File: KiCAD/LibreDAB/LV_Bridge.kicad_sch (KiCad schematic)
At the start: 68 parts, among them J1 HX PM2.54-1X4P TP H8.5-ZQ, J2 TS30050050-040, J3 TS30050050-040, J4 HX PM2.54-1X4P TP H8.5-ZQ, J5 HX PM2.54-1X4P TP H8.5-ZQ, J6 HX PM2.54-1X4P TP H8.5-ZQ, J7 TS30050050-040, J8 TS30050050-040, Q1 SP010N01BGHTO, Q2 SP010N01BGHTO, Q3 SP010N01BGHTO, Q4 SP010N01BGHTO, U2 10 MHz Opamp, U3 10 MHz Opamp, U4 10 MHz Opamp

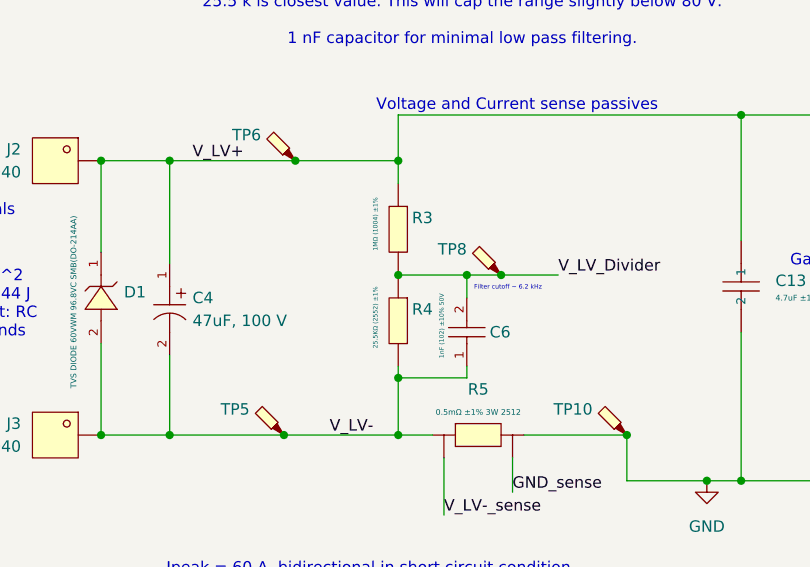
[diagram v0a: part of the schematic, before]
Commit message: Updated Voltage divider to 1206 for top half and 0.1%
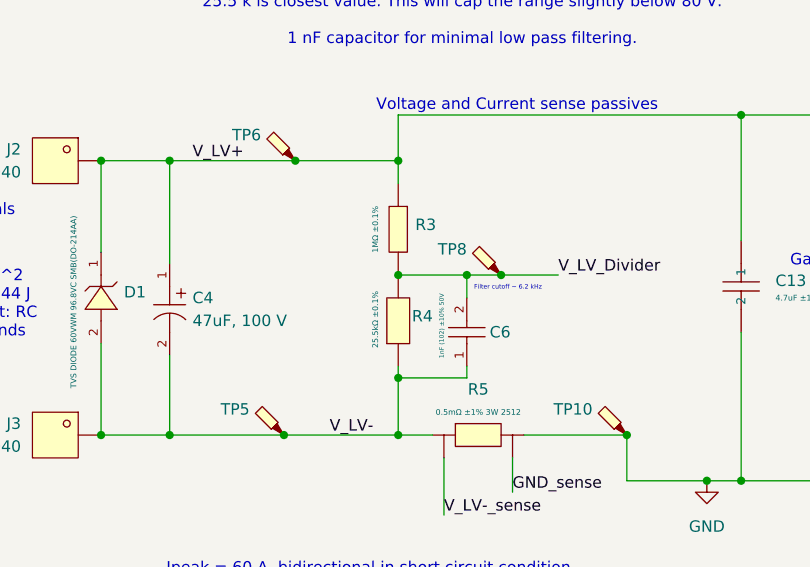
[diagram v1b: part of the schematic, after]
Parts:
- removed R3: 1MΩ (1004) ±1%, lcsc_footprints:C17514_R0805, symbol lcsc_imported:1MΩ_(1004)_±1%
- removed R4: 25.5KΩ (2552) ±1%, lcsc_footprints:C46670_R0805, symbol lcsc_imported:25_5KΩ_(2552)_±1%
- added R3: 1MΩ ±0.1%, lcsc_footprints:C309662_R1206, symbol lcsc_imported:RES 1MΩ ±0.1% 250mW 1206
- added R4: 25.5kΩ ±0.1%, lcsc_footprints:C865332_R0805, symbol lcsc_imported:RES 25.5kΩ ±0.1% 125mW 0805
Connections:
- net V_LV+: now also R3.1
- net V_LV-: now also R4.1
- net V_LV_Divider: now also R3.2, R4.2
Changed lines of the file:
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@@
 	)
 	(symbol
-		(lib_id "lcsc_imported:25_5KΩ_(2552)_±1%")
-		(at 82.55 81.28 270)
-		(unit 1)
-		(exclude_from_sim no)
-		(in_bom yes)
-		(on_board yes)
-		(dnp no)
-		(property "Reference" "R4"
-			(at 84.074 80.01 90)
-			(effects
-				(font
-					(size 1.27 1.27)
-				)
-				(justify left)
-			)
-		)
-		(property "Value" "25.5KΩ (2552) ±1%"
-			(at 80.01 77.47 0)
-			(effects
-				(font
-					(size 0.5 0.5)
-				)
-				(justify left)
-			)
-		)
-		(property "Footprint" "lcsc_footprints:C46670_R0805"
-			(at 72.39 81.28 0)
-			(effects
-				(font
-					(size 1.27 1.27)
-				)
-				(hide yes)
-			)
-		)
-		(property "Datasheet" "https://www.lcsc.com/datasheet/lcsc_datasheet_2206010000_UNI-ROYAL-Uniroyal-Elec-0805W8F2552T5E_C46670.pdf"
-			(at 82.677 78.994 0)
-			(effects
-				(font
-					(size 1.27 1.27)
-				)
-				(hide yes)
-			)
-		)
-		(property "Description" "25.5KΩ (2552) ±1%"
-			(at 82.55 81.28 0)
-			(effects
-				(font
-					(size 1.27 1.27)
-				)
-				(hide yes)
-			)
-		)
-		(property "LCSC" "C46670"
-			(at 82.55 81.28 0)
-			(effects
-				(font
-					(size 1.27 1.27)
-				)
-				(hide yes)
-			)
-		)
-		(property "Manufacturer" "UNI-ROYAL(厚声)"
-			(at 82.55 81.28 0)
-			(effects
-				(font
-					(size 1.27 1.27)
-				)
-				(hide yes)
-			)
-		)
-		(pin "1"
-		)
-		(pin "2"
-		)
-		(instances
-			(project "LibreDAB"
-				(path "/daf77073-b189-4351-8636-4e7a5198e1b7/f3c2518b-d41d-4c2c-ab2c-6739c5137e70"
-					(reference "R4")
-					(unit 1)
-				)
-			)
-		)
-	)
-	(symbol
 		(lib_id "lcsc_imported:HX_PM2_54-1X4P_TP_H8_5-ZQ")
 		(at 71.12 21.59 0)
@@
 	)
 	(symbol
+		(lib_id "lcsc_imported:RES 1MΩ ±0.1% 250mW 1206")
+		(at 82.55 71.12 270)
+		(unit 1)
+		(exclude_from_sim no)
+		(in_bom yes)
+		(on_board yes)
+		(dnp no)
+		(property "Reference" "R3"
+			(at 85.598 70.612 90)
+			(effects
+				(font
+					(size 1.27 1.27)
+				)
+			)
+		)
+		(property "Value" "1MΩ ±0.1%"
+			(at 80.01 71.12 0)
+			(effects
+				(font
+					(size 0.635 0.635)
+				)
+			)
+		)
+		(property "Footprint" "lcsc_footprints:C309662_R1206"
+			(at 72.39 71.12 0)
+			(effects
+				(font
+					(size 1.27 1.27)
+				)
+				(hide yes)
+			)
+		)
+		(property "Datasheet" "https://wmsc.lcsc.com/wmsc/upload/file/pdf/v2/lcsc/2304140030_YAGEO-RT1206BRD071ML_C309662.pdf"
+			(at 82.677 68.834 0)
+			(effects
+				(font
+					(size 1.27 1.27)
+				)
+				(hide yes)
+			)
+		)
+		(property "Description" "RT1206BRD071ML"
+			(at 82.55 71.12 0)
+			(effects
+				(font
+					(size 1.27 1.27)
+				)
+				(hide yes)
+			)
+		)
+		(property "LCSC" "C309662"
+			(at 82.55 71.12 0)
+			(effects
+				(font
+					(size 1.27 1.27)
+				)
+				(hide yes)
+			)
+		)
+		(property "Manufacturer" "YAGEO(国巨)"
+			(at 82.55 71.12 0)
+			(effects
+				(font
+					(size 1.27 1.27)
+				)
+				(hide yes)
+			)
+		)
+		(pin "2"
+		)
+		(pin "1"
+		)
+		(instances
+			(project ""
+				(path "/daf77073-b189-4351-8636-4e7a5198e1b7/f3c2518b-d41d-4c2c-ab2c-6739c5137e70"
+					(reference "R3")
+					(unit 1)
+				)
+			)
+		)
+	)
+	(symbol
 		(lib_id "power:GND")
 		(at 128.27 22.86 0)
@@
 	)
 	(symbol
-		(lib_id "lcsc_imported:1MΩ_(1004)_±1%")
-		(at 82.55 71.12 270)
-		(unit 1)
-		(exclude_from_sim no)
-		(in_bom yes)
-		(on_board yes)
-		(dnp no)
-		(property "Reference" "R3"
-			(at 84.074 69.85 90)
-			(effects
-				(font
-					(size 1.27 1.27)
-				)
-				(justify left)
-			)
-		)
-		(property "Value" "1MΩ (1004) ±1%"
-			(at 80.01 67.564 0)
-			(effects
-				(font
-					(size 0.5 0.5)
-				)
-				(justify left)
-			)
-		)
-		(property "Footprint" "lcsc_footprints:C17514_R0805"
-			(at 72.39 71.12 0)
-			(effects
-				(font
-					(size 1.27 1.27)
-				)
-				(hide yes)
-			)
-		)
-		(property "Datasheet" "https://www.lcsc.com/datasheet/lcsc_datasheet_2206010200_UNI-ROYAL-Uniroyal-Elec-0805W8F1004T5E_C17514.pdf"
-			(at 82.677 68.834 0)
-			(effects
-				(font
-					(size 1.27 1.27)
-				)
-				(hide yes)
-			)
-		)
-		(property "Description" "1MΩ (1004) ±1%"
-			(at 82.55 71.12 0)
-			(effects
-				(font
-					(size 1.27 1.27)
-				)
-				(hide yes)
-			)
-		)
-		(property "LCSC" "C17514"
-			(at 82.55 71.12 0)
-			(effects
-				(font
-					(size 1.27 1.27)
-				)
-				(hide yes)
-			)
-		)
-		(property "Manufacturer" "UNI-ROYAL(厚声)"
-			(at 82.55 71.12 0)
-			(effects
-				(font
-					(size 1.27 1.27)
-				)
-				(hide yes)
-			)
-		)
-		(pin "1"
-		)
-		(pin "2"
-		)
-		(instances
-			(project "LibreDAB"
-				(path "/daf77073-b189-4351-8636-4e7a5198e1b7/f3c2518b-d41d-4c2c-ab2c-6739c5137e70"
-					(reference "R3")
-					(unit 1)
-				)
-			)
-		)
-	)
-	(symbol
 		(lib_id "Connector:TestPoint_Probe")
 		(at 137.16 88.9 0)
@@
 					(unit 1)
 				)
+			)
+		)
+	)
+	(symbol
+		(lib_id "lcsc_imported:RES 25.5kΩ ±0.1% 125mW 0805")
+		(at 82.55 81.28 90)
+		(unit 1)
+		(exclude_from_sim no)
+		(in_bom yes)
+		(on_board yes)
+		(dnp no)
+		(property "Reference" "R4"
+			(at 84.074 80.772 90)
+			(effects
+				(font
+					(size 1.27 1.27)
+				)
+				(justify right)
+			)
+		)
+		(property "Value" "25.5kΩ ±0.1%"
+			(at 80.01 77.978 0)
+			(effects
+				(font
+					(size 0.635 0.635)
+				)
+				(justify right)
+			)
+		)
+		(property "Footprint" "lcsc_footprints:C865332_R0805"
+			(at 92.71 81.28 0)
+			(effects
+				(font
+					(size 1.27 1.27)
+				)
+				(hide yes)
+			)
+		)
+		(property "Datasheet" "https://wmsc.lcsc.com/wmsc/upload/file/pdf/v2/lcsc/2210081801_YAGEO-RT0805BRD0725K5L_C865332.pdf"
+			(at 82.423 83.566 0)
+			(effects
+				(font
+					(size 1.27 1.27)
+				)
+				(hide yes)
+			)
+		)
+		(property "Description" "RT0805BRD0725K5L"
+			(at 82.55 81.28 0)
+			(effects
+				(font
+					(size 1.27 1.27)
+				)
+				(hide yes)
+			)
+		)
+		(property "LCSC" "C865332"
+			(at 82.55 81.28 0)
+			(effects
+				(font
+					(size 1.27 1.27)
+				)
+				(hide yes)
+			)
+		)
+		(property "Manufacturer" "YAGEO(国巨)"
+			(at 82.55 81.28 0)
+			(effects
+				(font
+					(size 1.27 1.27)
+				)
+				(hide yes)
+			)
+		)
+		(pin "1"
+		)
+		(pin "2"
+		)
+		(instances
+			(project ""
+				(path "/daf77073-b189-4351-8636-4e7a5198e1b7/f3c2518b-d41d-4c2c-ab2c-6739c5137e70"
+					(reference "R4")
+					(unit 1)
+				)

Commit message: Review comments addressed or parked
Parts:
- H1, H2, H3, H4: footprint 1Footprints:MountingHole_Pad_SMD_BD5.6-D4.1 -> MountingHole:MountingHole_4.3mm_M4_DIN965_Pad
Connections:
- net V_LV-: now also R4.2; no longer R4.1
- net V_LV_Divider: now also R4.1; no longer R4.2
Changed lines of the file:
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@@
 	)
 	(junction
-		(at 82.55 76.2)
-		(diameter 0)
-		(color 0 0 0 0)
-	)
-	(junction
 		(at 26.6567 20.32)
 		(diameter 0)
@@
 	)
 	(junction
-		(at 82.55 87.63)
-		(diameter 0)
-		(color 0 0 0 0)
-	)
-	(junction
 		(at 177.8 153.67)
 		(diameter 0)
@@
 	)
 	(junction
+		(at 82.55 87.63)
+		(diameter 0)
+		(color 0 0 0 0)
+	)
+	(junction
 		(at 212.09 88.9)
 		(diameter 0)
@@
 	)
 	(junction
+		(at 82.55 76.2)
+		(diameter 0)
+		(color 0 0 0 0)
+	)
+	(junction
 		(at 57.15 63.5)
 		(diameter 0)
@@
 	(wire
 		(pts
+			(xy 82.55 86.36) (xy 82.55 87.63)
+		)
+		(stroke
+			(width 0)
+			(type default)
+		)
+	)
+	(wire
+		(pts
 			(xy 128.27 153.67) (xy 138.43 153.67)
 		)
@@
 	(wire
 		(pts
-			(xy 82.55 86.36) (xy 82.55 87.63)
-		)
-		(stroke
-			(width 0)
-			(type default)
-		)
-	)
-	(wire
-		(pts
 			(xy 196.85 24.13) (xy 199.39 24.13)
 		)
@@
 			)
 		)
-		(property "Footprint" "1Footprints:MountingHole_Pad_SMD_BD5.6-D4.1"
+		(property "Footprint" "MountingHole:MountingHole_4.3mm_M4_DIN965_Pad"
 			(at 138.43 172.72 0)
 			(effects
@@
 			)
 		)
-		(property "Footprint" "1Footprints:MountingHole_Pad_SMD_BD5.6-D4.1"
+		(property "Footprint" "MountingHole:MountingHole_4.3mm_M4_DIN965_Pad"
 			(at 152.4 172.72 0)
 			(effects
@@
 			)
 		)
-		(property "Footprint" "1Footprints:MountingHole_Pad_SMD_BD5.6-D4.1"
+		(property "Footprint" "MountingHole:MountingHole_4.3mm_M4_DIN965_Pad"
 			(at 138.43 185.42 0)
 			(effects
@@
 			)
 		)
-		(property "Footprint" "1Footprints:MountingHole_Pad_SMD_BD5.6-D4.1"
+		(property "Footprint" "MountingHole:MountingHole_4.3mm_M4_DIN965_Pad"
 			(at 152.4 185.42 0)
 			(effects
@@
 		(lib_id "lcsc_imported:RES 25.5kΩ ±0.1% 125mW 0805")
 		(at 82.55 81.28 90)
+		(mirror x)
 		(unit 1)
 		(exclude_from_sim no)
@@
 		(dnp no)
 		(property "Reference" "R4"
-			(at 84.074 80.772 90)
+			(at 84.074 81.788 90)
 			(effects
 				(font
@@
 		)
 		(property "Value" "25.5kΩ ±0.1%"
-			(at 80.01 77.978 0)
+			(at 80.01 84.582 0)
 			(effects
 				(font
@@
 		)
 		(property "Datasheet" "https://wmsc.lcsc.com/wmsc/upload/file/pdf/v2/lcsc/2210081801_YAGEO-RT0805BRD0725K5L_C865332.pdf"
-			(at 82.423 83.566 0)
+			(at 82.423 78.994 0)
 			(effects
 				(font
